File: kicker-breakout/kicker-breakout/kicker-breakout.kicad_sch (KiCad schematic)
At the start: 14 parts, among them J1 POWER, J2 DEV_BOARD, J3 KICKER_CONNECTION, Q1 BSS84

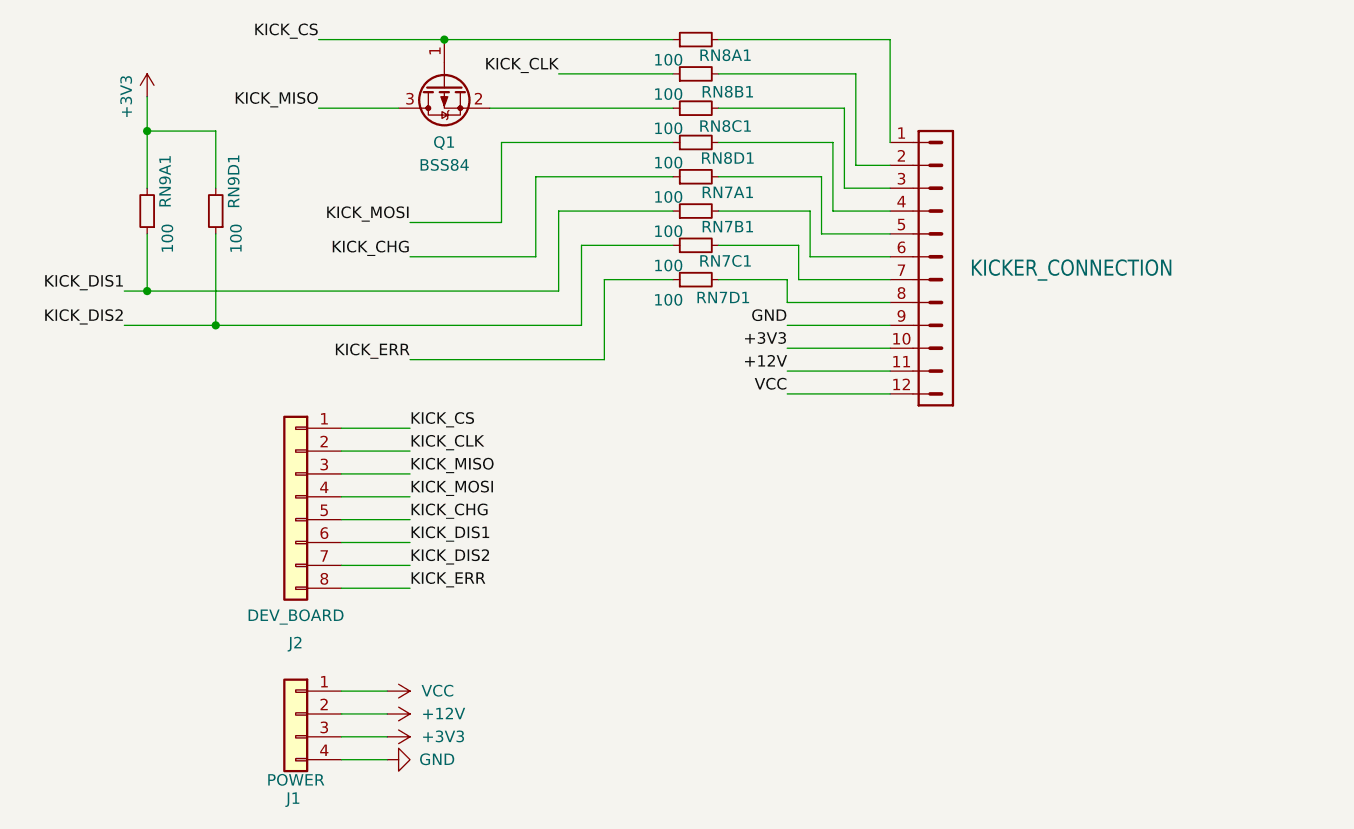
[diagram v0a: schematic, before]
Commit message: Add jlpcb design rules and fix incorrect pullup value
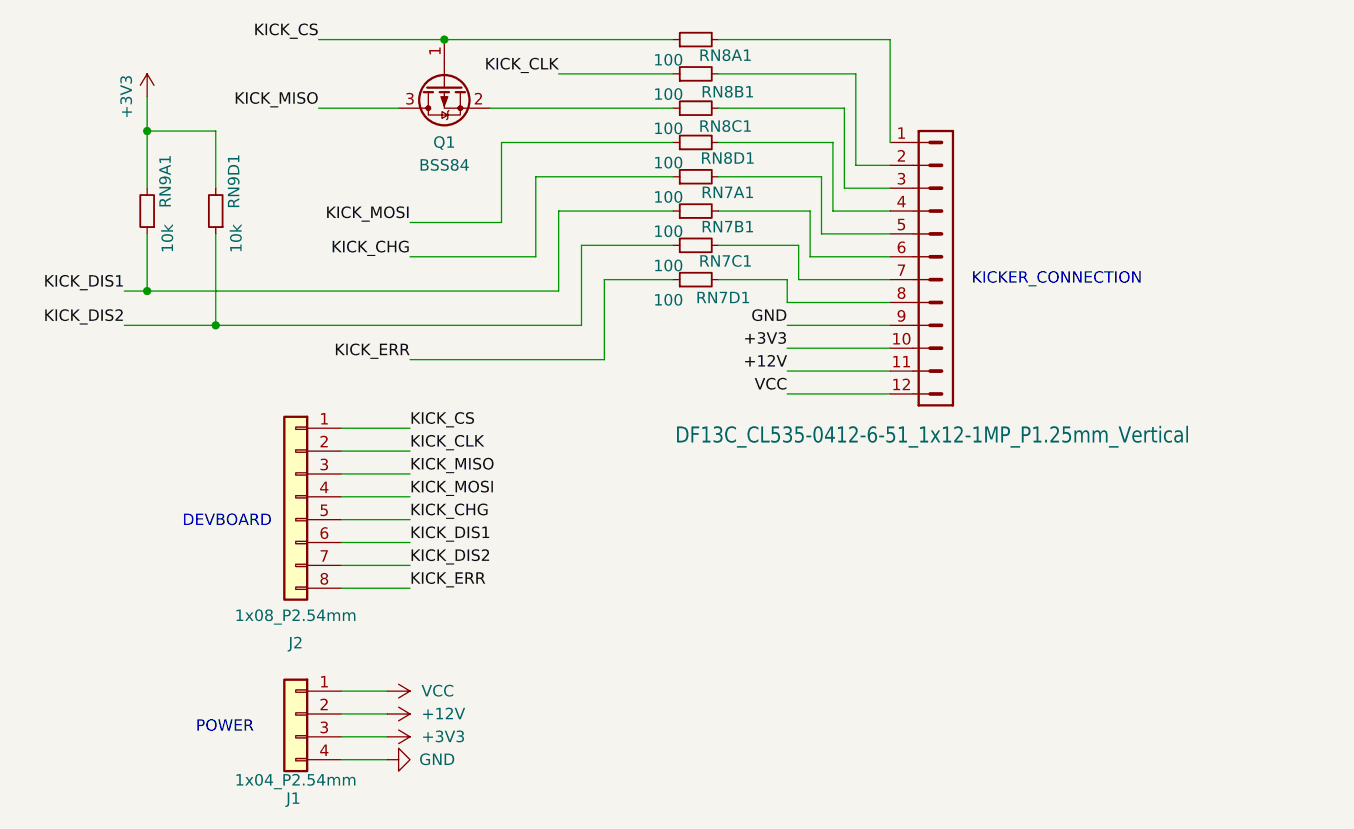
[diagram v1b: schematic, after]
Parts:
- J1: value POWER -> 1x04_P2.54mm
- J2: value DEV_BOARD -> 1x08_P2.54mm
- J3: value KICKER_CONNECTION -> DF13C_CL535-0412-6-51_1x12-1MP_P1.25mm_Vertical
- RN9A1, RN9D1: value 100 -> 10k
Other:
- note added: "DEVBOARD"
- note added: "KICKER_CONNECTION"
- note added: "POWER"
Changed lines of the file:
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@@
+		)
+	)
+	(text "POWER"
+		(exclude_from_sim no)
+		(at 58.166 101.854 0)
+		(effects
+			(font
+				(size 1.27 1.27)
+			)
+		)
+	)
+	(text "KICKER_CONNECTION"
+		(exclude_from_sim no)
+		(at 150.622 52.07 0)
+		(effects
+			(font
+				(size 1.27 1.27)
+			)
+		)
+	)
+	(text "DEVBOARD"
+		(exclude_from_sim no)
+		(at 58.42 78.994 0)
+		(effects
+			(font
+				(size 1.27 1.27)
+			)
 		)
 	)
@@
 			)
 		)
-		(property "Value" "DEV_BOARD"
+		(property "Value" "1x08_P2.54mm"
 			(at 66.04 89.408 0)
 			(effects
@@
 			)
 		)
-		(property "Value" "100"
+		(property "Value" "10k"
 			(at 59.436 47.498 90)
 			(effects
@@
 			)
 		)
-		(property "Value" "POWER"
+		(property "Value" "1x04_P2.54mm"
 			(at 66.04 107.696 0)
 			(effects
@@
 		(on_board yes)
 		(dnp no)
-		(fields_autoplaced yes)
 		(property "Reference" "J3"
 			(at 135.255 34.29 0)
@@
 			)
 		)
-		(property "Value" "KICKER_CONNECTION"
-			(at 140.97 50.8 0)
+		(property "Value" "DF13C_CL535-0412-6-51_1x12-1MP_P1.25mm_Vertical"
+			(at 108.204 69.342 0)
 			(effects
 				(font
@@
 			)
 		)
-		(property "Value" "100"
+		(property "Value" "10k"
 			(at 51.816 47.498 90)
 			(effects
